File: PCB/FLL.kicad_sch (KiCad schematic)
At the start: 9 parts, among them U1 MCP73831-2-MC, U3 LM317L_SOT-89

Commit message: chore: Update PCB design configuration and remove unnecessary files
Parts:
- added J1: Jack-DC, symbol Connector:Jack-DC
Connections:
- net +16V: no longer names the net of C3.2, U3.3 (VI)
- net +16V: now also J1.2
- net -16V renamed -7.5V
- net -7.5V: now also J1.1
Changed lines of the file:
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@@
+	(wire
+		(pts
+			(xy 86.36 129.54) (xy 121.92 129.54)
+		)
+		(stroke
+			(width 0)
+			(type default)
+		)
+	)
 	(wire
 		(pts
@@
 	(wire
 		(pts
+			(xy 86.36 124.46) (xy 97.79 124.46)
+		)
+		(stroke
+			(width 0)
+			(type default)
+		)
+	)
+	(wire
+		(pts
 			(xy 168.91 138.43) (xy 168.91 140.97)
 		)
@@
 	(wire
 		(pts
-			(xy 59.69 129.54) (xy 121.92 129.54)
-		)
-		(stroke
-			(width 0)
-			(type default)
-		)
-	)
-	(wire
-		(pts
 			(xy 121.92 83.82) (xy 124.46 83.82)
 		)
@@
 	(wire
 		(pts
-			(xy 59.69 99.06) (xy 59.69 129.54)
-		)
-		(stroke
-			(width 0)
-			(type default)
-		)
-	)
-	(wire
-		(pts
 			(xy 209.55 143.51) (xy 199.39 143.51)
 		)
@@
 	(wire
 		(pts
-			(xy 66.04 124.46) (xy 97.79 124.46)
-		)
-		(stroke
-			(width 0)
-			(type default)
-		)
-	)
-	(wire
-		(pts
 			(xy 142.24 83.82) (xy 142.24 86.36)
-		)
-		(stroke
-			(width 0)
-			(type default)
-		)
-	)
-	(wire
-		(pts
-			(xy 66.04 99.06) (xy 66.04 124.46)
 		)
 		(stroke
@@
 	)
 	(rectangle
-		(start 53.34 88.9)
-		(end 73.66 99.06)
+		(start 71.12 115.57)
+		(end 95.25 132.08)
 		(stroke
 			(width 0)
@@
 	(text "Powersupply 16V AC"
 		(exclude_from_sim no)
-		(at 63.246 91.186 0)
+		(at 83.312 117.348 0)
 		(effects
 			(font
@@
 	)
 	(symbol
-		(lib_id "power:+24V")
-		(at 59.69 99.06 0)
-		(unit 1)
-		(exclude_from_sim no)
-		(in_bom yes)
-		(on_board yes)
-		(dnp no)
-		(fields_autoplaced yes)
-		(property "Reference" "#PWR07"
-			(at 59.69 102.87 0)
-			(effects
-				(font
-					(size 1.27 1.27)
-				)
-				(hide yes)
-			)
-		)
-		(property "Value" "+16V"
-			(at 59.69 93.98 0)
-			(effects
-				(font
-					(size 1.27 1.27)
-				)
-			)
-		)
-		(property "Footprint" ""
-			(at 59.69 99.06 0)
-			(effects
-				(font
-					(size 1.27 1.27)
-				)
-				(hide yes)
-			)
-		)
-		(property "Datasheet" ""
-			(at 59.69 99.06 0)
-			(effects
-				(font
-					(size 1.27 1.27)
-				)
-				(hide yes)
-			)
-		)
-		(property "Description" "Power symbol creates a global label with name \"+24V\""
-			(at 59.69 99.06 0)
-			(effects
-				(font
-					(size 1.27 1.27)
-				)
-				(hide yes)
-			)
-		)
-		(pin "1"
-		)
-		(instances
-			(project ""
-				(path "/eebf961a-9e34-427c-a1d5-e0dfc5b48cc6"
-					(reference "#PWR07")
-					(unit 1)
-				)
-			)
-		)
-	)
-	(symbol
 		(lib_id "power:GND")
 		(at 115.57 62.23 180)
@@
 	)
 	(symbol
+		(lib_id "Connector:Jack-DC")
+		(at 78.74 127 0)
+		(unit 1)
+		(exclude_from_sim no)
+		(in_bom yes)
+		(on_board yes)
+		(dnp no)
+		(property "Reference" "J1"
+			(at 85.598 120.65 0)
+			(effects
+				(font
+					(size 1.27 1.27)
+				)
+			)
+		)
+		(property "Value" "Jack-DC"
+			(at 78.74 120.65 0)
+			(effects
+				(font
+					(size 1.27 1.27)
+				)
+			)
+		)
+		(property "Footprint" ""
+			(at 80.01 128.016 0)
+			(effects
+				(font
+					(size 1.27 1.27)
+				)
+				(hide yes)
+			)
+		)
+		(property "Datasheet" "~"
+			(at 80.01 128.016 0)
+			(effects
+				(font
+					(size 1.27 1.27)
+				)
+				(hide yes)
+			)
+		)
+		(property "Description" "DC Barrel Jack"
+			(at 78.74 127 0)
+			(effects
+				(font
+					(size 1.27 1.27)
+				)
+				(hide yes)
+			)
+		)
+		(pin "1"
+		)
+		(pin "2"
+		)
+		(instances
+			(project ""
+				(path "/eebf961a-9e34-427c-a1d5-e0dfc5b48cc6"
+					(reference "J1")
+					(unit 1)
+				)
+			)
+		)
+	)
+	(symbol
 		(lib_id "Device:R")
 		(at 142.24 90.17 0)
@@
 					(unit 1)
 				)
-			)
-		)
-	)
-	(symbol
-		(lib_id "power:-24V")
-		(at 66.04 99.06 0)
-		(unit 1)
-		(exclude_from_sim no)
-		(in_bom yes)
-		(on_board yes)
-		(dnp no)
-		(fields_autoplaced yes)
-		(property "Reference" "#PWR03"
-			(at 66.04 102.87 0)
-			(effects
-				(font
-					(size 1.27 1.27)
-				)
-				(hide yes)
-			)
-		)
-		(property "Value" "-16V"
-			(at 66.04 93.98 0)
-			(effects
-				(font
-					(size 1.27 1.27)
-				)
-			)
-		)
-		(property "Footprint" ""
-			(at 66.04 99.06 0)
-			(effects
-				(font
-					(size 1.27 1.27)
-				)
-				(hide yes)
-			)
-		)
-		(property "Datasheet" ""
-			(at 66.04 99.06 0)
-			(effects
-				(font
-					(size 1.27 1.27)
-				)
-				(hide yes)
-			)
-		)
-		(property "Description" "Power symbol creates a global label with name \"-24V\""
-			(at 66.04 99.06 0)
-			(effects
-				(font
-					(size 1.27 1.27)
-				)
-				(hide yes)
-			)
-		)
-		(pin "1"
-		)
-		(instances
-			(project ""
-				(path "/eebf961a-9e34-427c-a1d5-e0dfc5b48cc6"
-					(reference "#PWR03")
-					(unit 1)
-				)

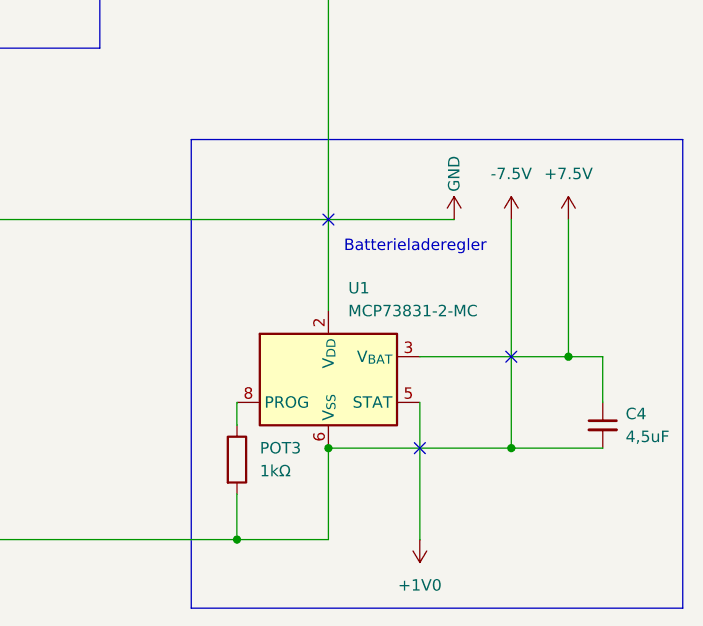
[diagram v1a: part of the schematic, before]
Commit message: deleted:    PCB/FLL-backups/FLL-2024-07-08_080917.zip
	new file:   PCB/FLL-backups/FLL-2024-07-09_095727.zip

	new file:   PCB/FLL-backups/FLL-2024-07-09_100644.zip

	modified:   PCB/FLL.kicad_sch
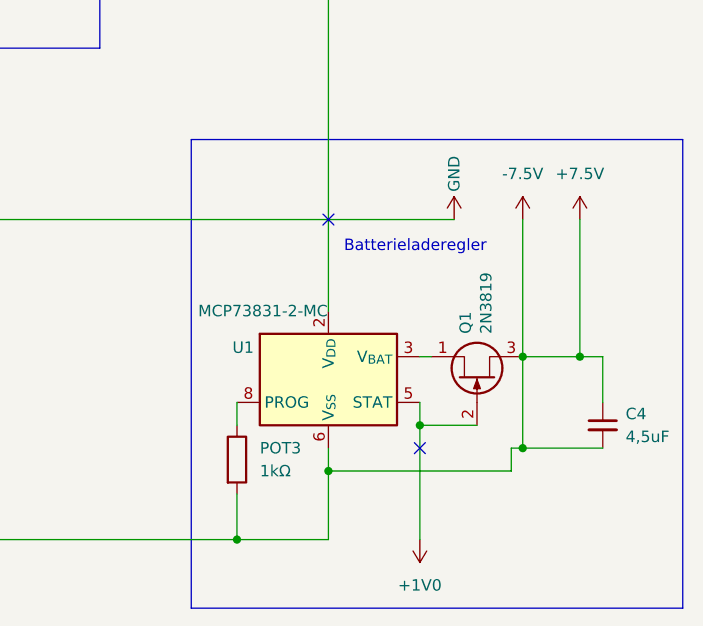
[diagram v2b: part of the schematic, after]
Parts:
- added Q1: 2N3819, Package_TO_SOT_THT:TO-92, symbol Transistor_FET:2N3819
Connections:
- net -7.5V is gone; now on net +7.5V: C4.2, J1.1, POT3.2, U1.6 (V_{SS})
- net +1V0: now also Q1.2 (G)
- net +7.5V: now also Q1.3 (S); no longer U1.3 (V_{BAT}), U1.4 (V_{BAT})
- new net: Q1.1 (D), U1.3 (V_{BAT}), U1.4 (V_{BAT})
- no-connect marks 6 -> 5
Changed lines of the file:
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@@
+	)
+	(junction
+		(at 200.66 133.35)
+		(diameter 0)
+		(color 0 0 0 0)
 	)
 	(junction
@@
 	)
 	(junction
-		(at 205.74 133.35)
-		(diameter 0)
-		(color 0 0 0 0)
-	)
-	(junction
-		(at 179.07 143.51)
+		(at 179.07 146.05)
 		(diameter 0)
 		(color 0 0 0 0)
@@
 	)
 	(junction
+		(at 200.66 143.51)
+		(diameter 0)
+		(color 0 0 0 0)
+	)
+	(junction
+		(at 189.23 140.97)
+		(diameter 0)
+		(color 0 0 0 0)
+	)
+	(junction
 		(at 132.08 93.98)
 		(diameter 0)
@@
 	)
 	(junction
-		(at 199.39 143.51)
+		(at 207.01 133.35)
 		(diameter 0)
 		(color 0 0 0 0)
@@
 	)
 	(no_connect
-		(at 199.39 133.35)
-	)
-	(no_connect
 		(at 179.07 118.11)
 	)
@@
 	(wire
 		(pts
-			(xy 209.55 133.35) (xy 205.74 133.35)
+			(xy 209.55 133.35) (xy 207.01 133.35)
 		)
 		(stroke
@@
 	(wire
 		(pts
-			(xy 205.74 118.11) (xy 205.74 133.35)
+			(xy 189.23 138.43) (xy 189.23 140.97)
+		)
+		(stroke
+			(width 0)
+			(type default)
+		)
+	)
+	(wire
+		(pts
+			(xy 207.01 118.11) (xy 207.01 133.35)
 		)
 		(stroke
@@
 	(wire
 		(pts
-			(xy 179.07 153.67) (xy 179.07 143.51)
+			(xy 179.07 153.67) (xy 179.07 146.05)
 		)
 		(stroke
@@
 	(wire
 		(pts
+			(xy 189.23 140.97) (xy 189.23 153.67)
+		)
+		(stroke
+			(width 0)
+			(type default)
+		)
+	)
+	(wire
+		(pts
 			(xy 115.57 97.79) (xy 123.19 97.79)
 		)
@@
 	(wire
 		(pts
-			(xy 209.55 143.51) (xy 199.39 143.51)
-		)
-		(stroke
-			(width 0)
-			(type default)
-		)
-	)
-	(wire
-		(pts
-			(xy 189.23 138.43) (xy 189.23 153.67)
+			(xy 209.55 143.51) (xy 200.66 143.51)
 		)
 		(stroke
@@
 	(wire
 		(pts
-			(xy 199.39 118.11) (xy 199.39 143.51)
+			(xy 200.66 118.11) (xy 200.66 133.35)
+		)
+		(stroke
+			(width 0)
+			(type default)
+		)
+	)
+	(wire
+		(pts
+			(xy 179.07 146.05) (xy 179.07 143.51)
 		)
 		(stroke
@@
 	(wire
 		(pts
+			(xy 200.66 143.51) (xy 199.39 143.51)
+		)
+		(stroke
+			(width 0)
+			(type default)
+		)
+	)
+	(wire
+		(pts
 			(xy 152.4 83.82) (xy 152.4 76.2)
 		)
@@
 	(wire
 		(pts
-			(xy 179.07 143.51) (xy 199.39 143.51)
+			(xy 179.07 146.05) (xy 199.39 146.05)
 		)
 		(stroke
@@
 	(wire
 		(pts
+			(xy 200.66 133.35) (xy 200.66 143.51)
+		)
+		(stroke
+			(width 0)
+			(type default)
+		)
+	)
+	(wire
+		(pts
 			(xy 168.91 153.67) (xy 179.07 153.67)
 		)
@@
 	(wire
 		(pts
+			(xy 200.66 133.35) (xy 207.01 133.35)
+		)
+		(stroke
+			(width 0)
+			(type default)
+		)
+	)
+	(wire
+		(pts
 			(xy 179.07 83.82) (xy 179.07 128.27)
 		)
@@
 	(wire
 		(pts
-			(xy 189.23 133.35) (xy 205.74 133.35)
+			(xy 195.58 140.97) (xy 189.23 140.97)
 		)
 		(stroke
@@
 	(wire
 		(pts
+			(xy 199.39 146.05) (xy 199.39 143.51)
+		)
+		(stroke
+			(width 0)
+			(type default)
+		)
+	)
+	(wire
+		(pts
 			(xy 116.84 83.82) (xy 115.57 83.82)
 		)
@@
 		(pts
 			(xy 132.08 93.98) (xy 132.08 97.79)
+		)
+		(stroke
+			(width 0)
+			(type default)
+		)
+	)
+	(wire
+		(pts
+			(xy 190.5 133.35) (xy 189.23 133.35)
 		)
 		(stroke
@@
 			)
 		)
-		(property "Datasheet" "~"
+		(property "Datasheet" "240Ω"
 			(at 142.24 90.17 0)
 			(effects
@@
 	(symbol
 		(lib_id "power:+7.5V")
-		(at 205.74 118.11 0)
+		(at 207.01 118.11 0)
 		(unit 1)
 		(exclude_from_sim no)
@@
 		(fields_autoplaced yes)
 		(property "Reference" "#PWR02"
-			(at 205.74 121.92 0)
+			(at 207.01 121.92 0)
 			(effects
 				(font
@@
 		)
 		(property "Value" "+7.5V"
-			(at 205.74 113.03 0)
+			(at 207.01 113.03 0)
 			(effects
 				(font
@@
 		)
 		(property "Footprint" ""
-			(at 205.74 118.11 0)
+			(at 207.01 118.11 0)
 			(effects
 				(font
@@
 		)
 		(property "Datasheet" ""
-			(at 205.74 118.11 0)
+			(at 207.01 118.11 0)
 			(effects
 				(font
@@
 		)
 		(property "Description" "Power symbol creates a global label with name \"+7.5V\""
-			(at 205.74 118.11 0)
+			(at 207.01 118.11 0)
 			(effects
 				(font
@@
 	(symbol
 		(lib_id "power:+7.5V")
-		(at 199.39 118.11 0)
+		(at 200.66 118.11 0)
 		(unit 1)
 		(exclude_from_sim no)
@@
 		(fields_autoplaced yes)
 		(property "Reference" "#PWR04"
-			(at 199.39 121.92 0)
+			(at 200.66 121.92 0)
 			(effects
 				(font
@@
 		)
 		(property "Value" "-7.5V"
-			(at 199.39 113.03 0)
+			(at 200.66 113.03 0)
 			(effects
 				(font
@@
 		)
 		(property "Footprint" ""
-			(at 199.39 118.11 0)
+			(at 200.66 118.11 0)
 			(effects
 				(font
@@
 		)
 		(property "Datasheet" ""
-			(at 199.39 118.11 0)
+			(at 200.66 118.11 0)
 			(effects
 				(font
@@
 		)
 		(property "Description" "Power symbol creates a global label with name \"+7.5V\""
-			(at 199.39 118.11 0)
+			(at 200.66 118.11 0)
 			(effects
 				(font
@@
 		(on_board yes)
 		(dnp no)
-		(fields_autoplaced yes)
 		(property "Reference" "U1"
-			(at 181.2641 125.73 0)
+			(at 168.402 132.334 0)
 			(effects
 				(font
@@
 		)
 		(property "Value" "MCP73831-2-MC"
-			(at 181.2641 128.27 0)
+			(at 164.592 128.27 0)
 			(effects
 				(font
@@
 	)
 	(symbol
+		(lib_id "Transistor_FET:2N3819")
+		(at 195.58 135.89 90)
+		(unit 1)
+		(exclude_from_sim no)
+		(in_bom yes)
+		(on_board yes)
+		(dnp no)
+		(property "Reference" "Q1"
+			(at 194.3099 130.81 0)
+			(effects
+				(font
+					(size 1.27 1.27)
+				)
+				(justify left)
+			)
+		)
+		(property "Value" "2N3819"
+			(at 196.596 130.81 0)
+			(effects
+				(font
+					(size 1.27 1.27)
+				)
+				(justify left)
+			)
+		)
+		(property "Footprint" "Package_TO_SOT_THT:TO-92"
+			(at 197.485 130.81 0)
+			(effects
+				(font
+					(size 1.27 1.27)
+					(italic yes)
+				)
+				(justify left)
+				(hide yes)
+			)
+		)
+		(property "Datasheet" "https://my.centralsemi.com/datasheets/2N3819.PDF"
+			(at 199.39 130.81 0)
+			(effects
+				(font
+					(size 1.27 1.27)
+				)
+				(justify left)
+				(hide yes)
+			)
+		)
+		(property "Description" "20mA Id, 25V Vgs, N-Channel JFET Transistor, TO-92"
+			(at 195.58 135.89 0)
+			(effects
+				(font
+					(size 1.27 1.27)
+				)
+				(hide yes)
+			)
+		)
+		(pin "1"
+		)
+		(pin "2"
+		)
+		(pin "3"
+		)
+		(instances
+			(project ""
+				(path "/eebf961a-9e34-427c-a1d5-e0dfc5b48cc6"
+					(reference "Q1")
+					(unit 1)
+				)
+			)
+		)
+	)
+	(symbol
 		(lib_id "Device:R")
 		(at 127 97.79 90)
@@
 			)
 		)
-		(property "Datasheet" "~"
+		(property "Datasheet" "1,4kΩ"
 			(at 127 97.79 0)
 			(effects

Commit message: chore: Update PCB design configuration and remove unnecessary files
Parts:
- removed Q1: 2N3819, Package_TO_SOT_THT:TO-92, symbol Transistor_FET:2N3819
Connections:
- net +7.5V: now also U1.3 (V_{BAT}), U1.4 (V_{BAT}); no longer C4.2, J1.1, POT3.2, U1.6 (V_{SS})
- new net -7.5V: C4.2, J1.1, POT3.2, U1.6 (V_{SS})
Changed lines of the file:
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@@
-	)
-	(junction
-		(at 200.66 133.35)
-		(diameter 0)
-		(color 0 0 0 0)
 	)
 	(junction
@@
 	)
 	(junction
-		(at 179.07 146.05)
+		(at 179.07 143.51)
 		(diameter 0)
 		(color 0 0 0 0)
@@
 	)
 	(junction
-		(at 189.23 140.97)
+		(at 207.01 133.35)
 		(diameter 0)
 		(color 0 0 0 0)
@@
 	)
 	(junction
-		(at 207.01 133.35)
-		(diameter 0)
-		(color 0 0 0 0)
-	)
-	(junction
 		(at 115.57 97.79)
 		(diameter 0)
@@
 	(wire
 		(pts
-			(xy 189.23 138.43) (xy 189.23 140.97)
-		)
-		(stroke
-			(width 0)
-			(type default)
-		)
-	)
-	(wire
-		(pts
 			(xy 207.01 118.11) (xy 207.01 133.35)
 		)
@@
 	(wire
 		(pts
-			(xy 179.07 153.67) (xy 179.07 146.05)
-		)
-		(stroke
-			(width 0)
-			(type default)
-		)
-	)
-	(wire
-		(pts
 			(xy 140.97 76.2) (xy 115.57 76.2)
 		)
@@
 	(wire
 		(pts
-			(xy 189.23 140.97) (xy 189.23 153.67)
+			(xy 189.23 138.43) (xy 189.23 153.67)
 		)
 		(stroke
@@
 	(wire
 		(pts
+			(xy 189.23 133.35) (xy 207.01 133.35)
+		)
+		(stroke
+			(width 0)
+			(type default)
+		)
+	)
+	(wire
+		(pts
 			(xy 209.55 143.51) (xy 200.66 143.51)
 		)
@@
 	(wire
 		(pts
-			(xy 200.66 118.11) (xy 200.66 133.35)
-		)
-		(stroke
-			(width 0)
-			(type default)
-		)
-	)
-	(wire
-		(pts
-			(xy 179.07 146.05) (xy 179.07 143.51)
+			(xy 200.66 118.11) (xy 200.66 143.51)
+		)
+		(stroke
+			(width 0)
+			(type default)
+		)
+	)
+	(wire
+		(pts
+			(xy 179.07 143.51) (xy 179.07 153.67)
 		)
 		(stroke
@@
 	(wire
 		(pts
-			(xy 200.66 143.51) (xy 199.39 143.51)
-		)
-		(stroke
-			(width 0)
-			(type default)
-		)
-	)
-	(wire
-		(pts
 			(xy 152.4 83.82) (xy 152.4 76.2)
 		)
@@
 	(wire
 		(pts
-			(xy 179.07 146.05) (xy 199.39 146.05)
+			(xy 179.07 143.51) (xy 200.66 143.51)
 		)
 		(stroke
@@
 	(wire
 		(pts
-			(xy 200.66 133.35) (xy 200.66 143.51)
-		)
-		(stroke
-			(width 0)
-			(type default)
-		)
-	)
-	(wire
-		(pts
 			(xy 168.91 153.67) (xy 179.07 153.67)
 		)
@@
 	(wire
 		(pts
-			(xy 200.66 133.35) (xy 207.01 133.35)
-		)
-		(stroke
-			(width 0)
-			(type default)
-		)
-	)
-	(wire
-		(pts
 			(xy 179.07 83.82) (xy 179.07 128.27)
 		)
@@
 	(wire
 		(pts
-			(xy 195.58 140.97) (xy 189.23 140.97)
-		)
-		(stroke
-			(width 0)
-			(type default)
-		)
-	)
-	(wire
-		(pts
 			(xy 142.24 83.82) (xy 142.24 86.36)
 		)
@@
 	(wire
 		(pts
-			(xy 199.39 146.05) (xy 199.39 143.51)
-		)
-		(stroke
-			(width 0)
-			(type default)
-		)
-	)
-	(wire
-		(pts
 			(xy 116.84 83.82) (xy 115.57 83.82)
 		)
@@
 		(pts
 			(xy 132.08 93.98) (xy 132.08 97.79)
-		)
-		(stroke
-			(width 0)
-			(type default)
-		)
-	)
-	(wire
-		(pts
-			(xy 190.5 133.35) (xy 189.23 133.35)
 		)
 		(stroke
@@
 					(unit 1)
 				)
-			)
-		)
-	)
-	(symbol
-		(lib_id "Transistor_FET:2N3819")
-		(at 195.58 135.89 90)
-		(unit 1)
-		(exclude_from_sim no)
-		(in_bom yes)
-		(on_board yes)
-		(dnp no)
-		(property "Reference" "Q1"
-			(at 194.3099 130.81 0)
-			(effects
-				(font
-					(size 1.27 1.27)
-				)
-				(justify left)
-			)
-		)
-		(property "Value" "2N3819"
-			(at 196.596 130.81 0)
-			(effects
-				(font
-					(size 1.27 1.27)
-				)
-				(justify left)
-			)
-		)
-		(property "Footprint" "Package_TO_SOT_THT:TO-92"
-			(at 197.485 130.81 0)
-			(effects
-				(font
-					(size 1.27 1.27)
-					(italic yes)
-				)
-				(justify left)
-				(hide yes)
-			)
-		)
-		(property "Datasheet" "https://my.centralsemi.com/datasheets/2N3819.PDF"
-			(at 199.39 130.81 0)
-			(effects
-				(font
-					(size 1.27 1.27)
-				)
-				(justify left)
-				(hide yes)
-			)
-		)
-		(property "Description" "20mA Id, 25V Vgs, N-Channel JFET Transistor, TO-92"
-			(at 195.58 135.89 0)
-			(effects
-				(font
-					(size 1.27 1.27)
-				)
-				(hide yes)
-			)
-		)
-		(pin "1"
-		)
-		(pin "2"
-		)
-		(pin "3"
-		)
-		(instances
-			(project ""
-				(path "/eebf961a-9e34-427c-a1d5-e0dfc5b48cc6"
-					(reference "Q1")
-					(unit 1)
-				)
